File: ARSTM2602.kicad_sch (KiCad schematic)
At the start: 0 parts

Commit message: aaa
gitdesktop test
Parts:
- added U1: STM32H523CCTx, Package_QFP:LQFP-48_7x7mm_P0.5mm, symbol MCU_ST_STM32H5:STM32H523CCTx
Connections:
- new net: U1.23 (VSS), U1.35 (VSS), U1.47 (VSS)
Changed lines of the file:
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@@
 (kicad_sch
-	(version 20250114)
+	(version 20260306)
 	(generator "eeschema")
-	(generator_version "9.0")
+	(generator_version "10.0")
 	(paper "A4")
-	(sheet_instances
-		(path "/"
-			(page "1")
-		)
-	)
-	(embedded_fonts no)
-)

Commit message: 回路図をこぴった
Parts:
- removed U1: STM32H523CCTx, Package_QFP:LQFP-48_7x7mm_P0.5mm, symbol MCU_ST_STM32H5:STM32H523CCTx
- added C1, C17: 22μF, Capacitor_SMD:C_0805_2012Metric_Pad1.18x1.45mm_HandSolder, symbol Device:C
- added C10: 4.7uf, Capacitor_SMD:C_0805_2012Metric_Pad1.18x1.45mm_HandSolder, symbol Device:C
- added C11, C7, C8, C9: 0.1uF, Capacitor_SMD:C_0603_1608Metric_Pad1.08x0.95mm_HandSolder, symbol Device:C
- added C12, C4: 0.1uf, Capacitor_SMD:C_0603_1608Metric_Pad1.08x0.95mm_HandSolder, symbol Device:C
- added C13, C14: 1uf, Capacitor_SMD:C_0603_1608Metric_Pad1.08x0.95mm_HandSolder, symbol Device:C
- added C15, C16, C2, C3: 4.7μF, Capacitor_SMD:C_0805_2012Metric_Pad1.18x1.45mm_HandSolder, symbol Device:C
- added C5, C6: 2.2μF, Capacitor_SMD:C_0603_1608Metric_Pad1.08x0.95mm_HandSolder, symbol Device:C
- added D2, D4: D_Shockley, Diode_SMD:D_SOD-323_HandSoldering, symbol Device:D_Shockley
- added D3: LED_GREEN, Capacitor_SMD:C_0603_1608Metric_Pad1.08x0.95mm_HandSolder, symbol Device:LED
- added J10: USB_C_Receptacle_USB2.0_16P, Connector_USB:USB_C_Receptacle_GCT_USB4105-xx-A_16P_TopMnt_Horizontal, symbol Connector:USB_C_Receptacle_USB2.0_16P
- added J4, J5: Conn_01x02_Socket, Connector_JST:JST_XH_S2B-XH-A-1_1x02_P2.50mm_Horizontal, symbol Connector:Conn_01x02_Socket
- added J9: Conn_ST_STDC14, Connector_PinHeader_1.27mm:PinHeader_2x07_P1.27mm_Vertical, symbol Connector:Conn_ST_STDC14
- added R10, R9: 5.1k, Resistor_SMD:R_0603_1608Metric_Pad0.98x0.95mm_HandSolder, symbol Device:R
- added R4: 120, Resistor_SMD:R_0603_1608Metric_Pad0.98x0.95mm_HandSolder, symbol Device:R
- added R5: 10K, Resistor_SMD:R_0603_1608Metric_Pad0.98x0.95mm_HandSolder, symbol Device:R
- added R7: 1k, Resistor_SMD:R_0603_1608Metric_Pad0.98x0.95mm_HandSolder, symbol Device:R
- added SW1: SW_Wuerth_450301014042, Button_Switch_THT:SW_Slide-03_Wuerth-WS-SLTV_10x2.5x6.4_P2.54mm, symbol Switch:SW_Wuerth_450301014042
- added SW2: SW_SPDT, Button_Switch_THT:SW_Slide-03_Wuerth-WS-SLTV_10x2.5x6.4_P2.54mm, symbol Switch:SW_SPDT
- added SW3: SW_Push, Button_Switch_THT:SW_PUSH_6mm, symbol Switch:SW_Push
- added U1: BD50FC0FP, Package_TO_SOT_SMD:TO-252-2, symbol Regulator_Linear:BD50FC0FP
- added U3: MCP2562-E-P, Package_DIP:DIP-8_W7.62mm, symbol Interface_CAN_LIN:MCP2562-E-P
- added U4: STM32H523CCTx, Package_QFP:LQFP-48_7x7mm_P0.5mm, symbol MCU_ST_STM32H5:STM32H523CCTx
- added U5: BD33FC0FP, Package_TO_SOT_SMD:TO-252-2, symbol Regulator_Linear:BD33FC0FP
- added U6: CH340E, Package_SO:MSOP-10_3x3mm_P0.5mm, symbol Interface_USB:CH340E
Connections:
- new net: D3.1 (K), R7.2
- new net: C6.2, U4.46 (VCAP)
- new net: C5.2, U4.22 (VCAP)
- new net: J10.A5 (CC1), R10.1
- new net: J10.B5 (CC2), R9.1
- new net: D3.2 (A), U4.11 (PA1)
- new net: C14.1, U6.10 (V3)
- new net +24V: C2.1, D2.1 (K), U1.1 (VCC)
- new net +3.3V: C10.1, C11.1, C12.2, C13.2, C16.1, C17.1, C7.1, C8.1, C9.1, D4.2 (A), J9.3 (VCC), U3.5 (Vio), U4.1 (VBAT), U4.24 (VDD), U4.36 (VDD), U4.48 (VDD), U4.9 (VDDA), U5.3 (VO)
- new net +5V: C1.1, C15.1, C3.1, C4.1, D2.2 (A), D4.1 (K), J10.A4 (VBUS), J10.A9 (VBUS), J10.B4 (VBUS), J10.B9 (VBUS), U1.3 (VO), U3.3 (VDD), U5.1 (VCC), U6.7 (VCC)
- new net BOOT0: R5.1, SW2.2 (B), U4.44 (BOOT0)
- new net CAN2rx: U3.4 (RXD), U4.32 (PA11)
- new net CAN2tx: U3.1 (TXD), U4.33 (PA12)
- new net CANR: R4.2, SW1.3 (A)
- new net CAN_H: J4.2 (Pin_2), J5.2 (Pin_2), SW1.1 (B), U3.7 (CANH)
- new net CAN_L: J4.1 (Pin_1), J5.1 (Pin_1), R4.1, U3.6 (CANL)
- new net GND: C1.2, C10.2, C11.2, C12.1, C13.1, C14.2, C15.2, C16.2, C17.2, C2.2, C3.2, C4.2, C5.1, C6.1, C7.2, C8.2, C9.2, J10.A1 (GND), J10.A12 (GND), J10.B1 (GND), J10.B12 (GND), J10.S1 (SHIELD), J9.5 (GND), J9.7 (GND), R10.2, R5.2, R7.1, R9.2, SW2.1 (A), SW3.2, U1.2 (GND), U3.2 (VSS), U3.8 (STBY), U4.23 (VSS), U4.35 (VSS), U4.47 (VSS), U4.8 (VSSA), U5.2 (GND), U6.3 (GND)
- new net d+: J10.A7 (D-), J10.B7 (D-), U6.1 (UD+)
- new net d-: J10.A6 (D+), J10.B6 (D+), U6.2 (UD-)
- new net jtdi: J9.10 (JTDI/NC), U4.38 (PA15(JTDI))
- new net nrst: SW3.1, U4.7 (NRST)
- new net swclk: J9.6 (JCLK/SWCLK), U4.37 (PA14(JTCK)
- new net swdio: J9.4 (JTMS/SWDIO), U4.34 (PA13(JTMS)
- new net swo: J9.8 (JTDO/SWO), U4.39 (PB3(JTDO)
- new net trst: J9.12 (~{RST}), U4.40 (PB4(NJTRST))
- new net uart1-rx: J9.13 (VCP_RX), U4.43 (PB7), U6.9 (RXD)
- new net uart1-tx: J9.14 (VCP_TX), U4.42 (PB6), U6.8 (TXD)
- no-connect marks 0 -> 9
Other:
- note added: "CANトランシーバー"
- note added: "STlink,電源供給usbC"
- note added: "リセット用スイッチ"
- note added: "終端抵抗オンオフ"

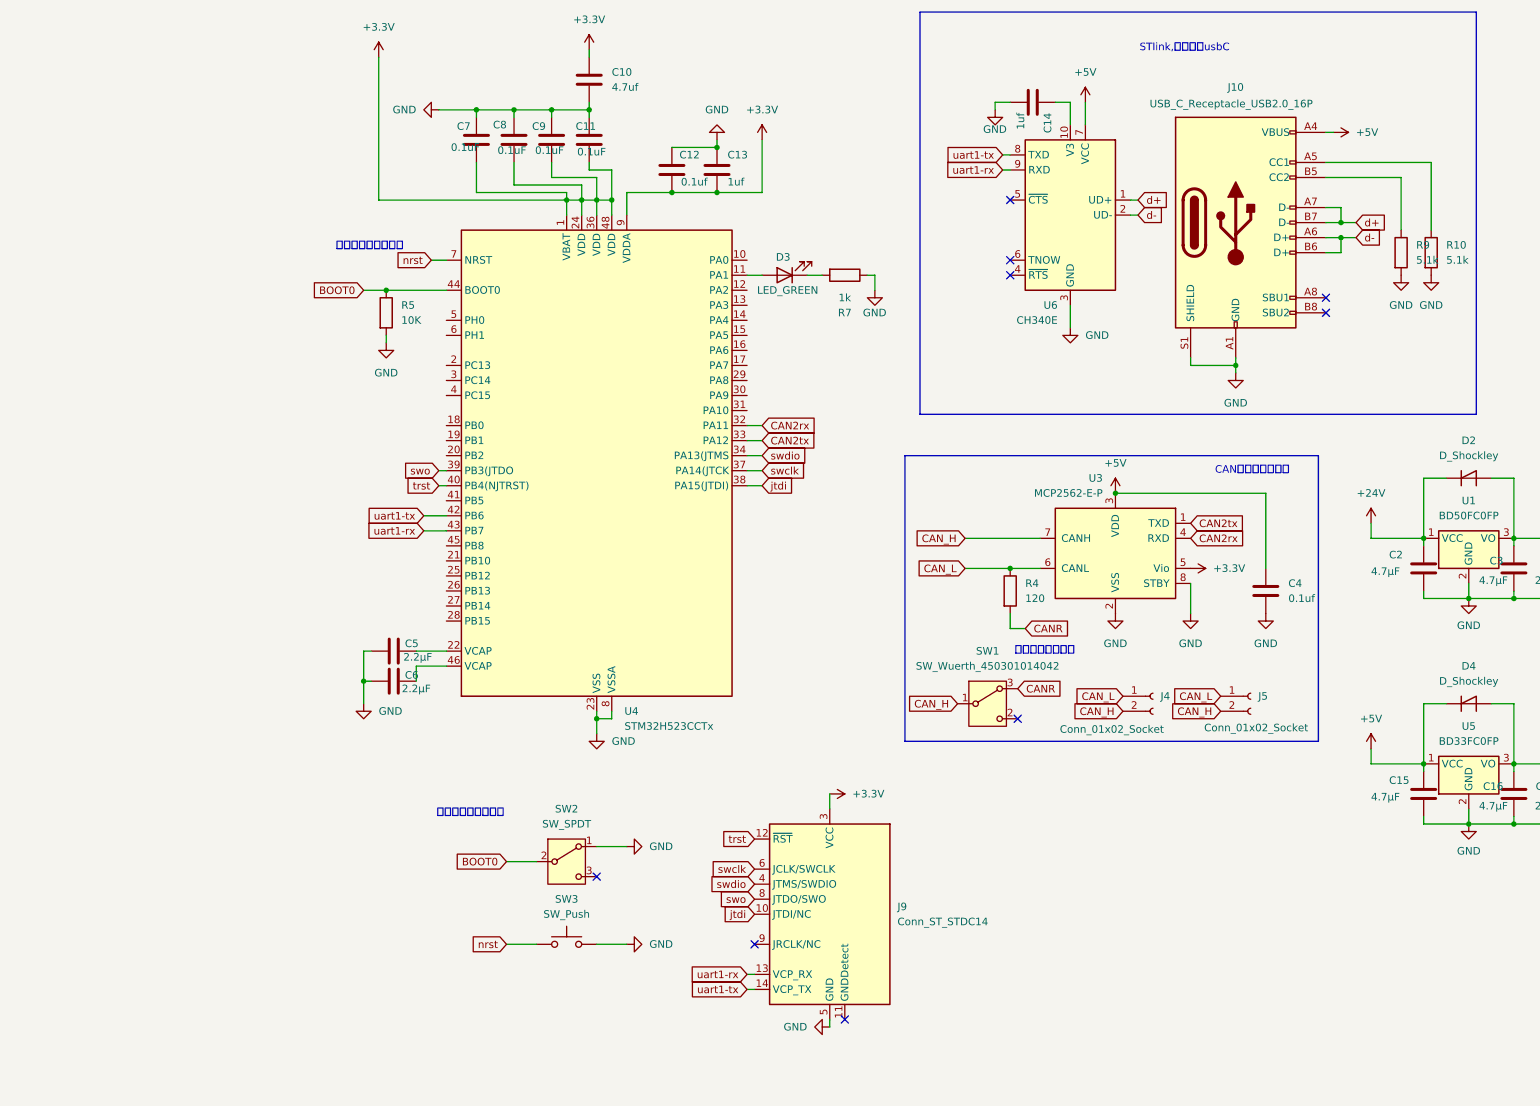
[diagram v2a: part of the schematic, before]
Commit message: canモジュールを増やした
電源供給方法をいろいろ考えついたから頑張る()
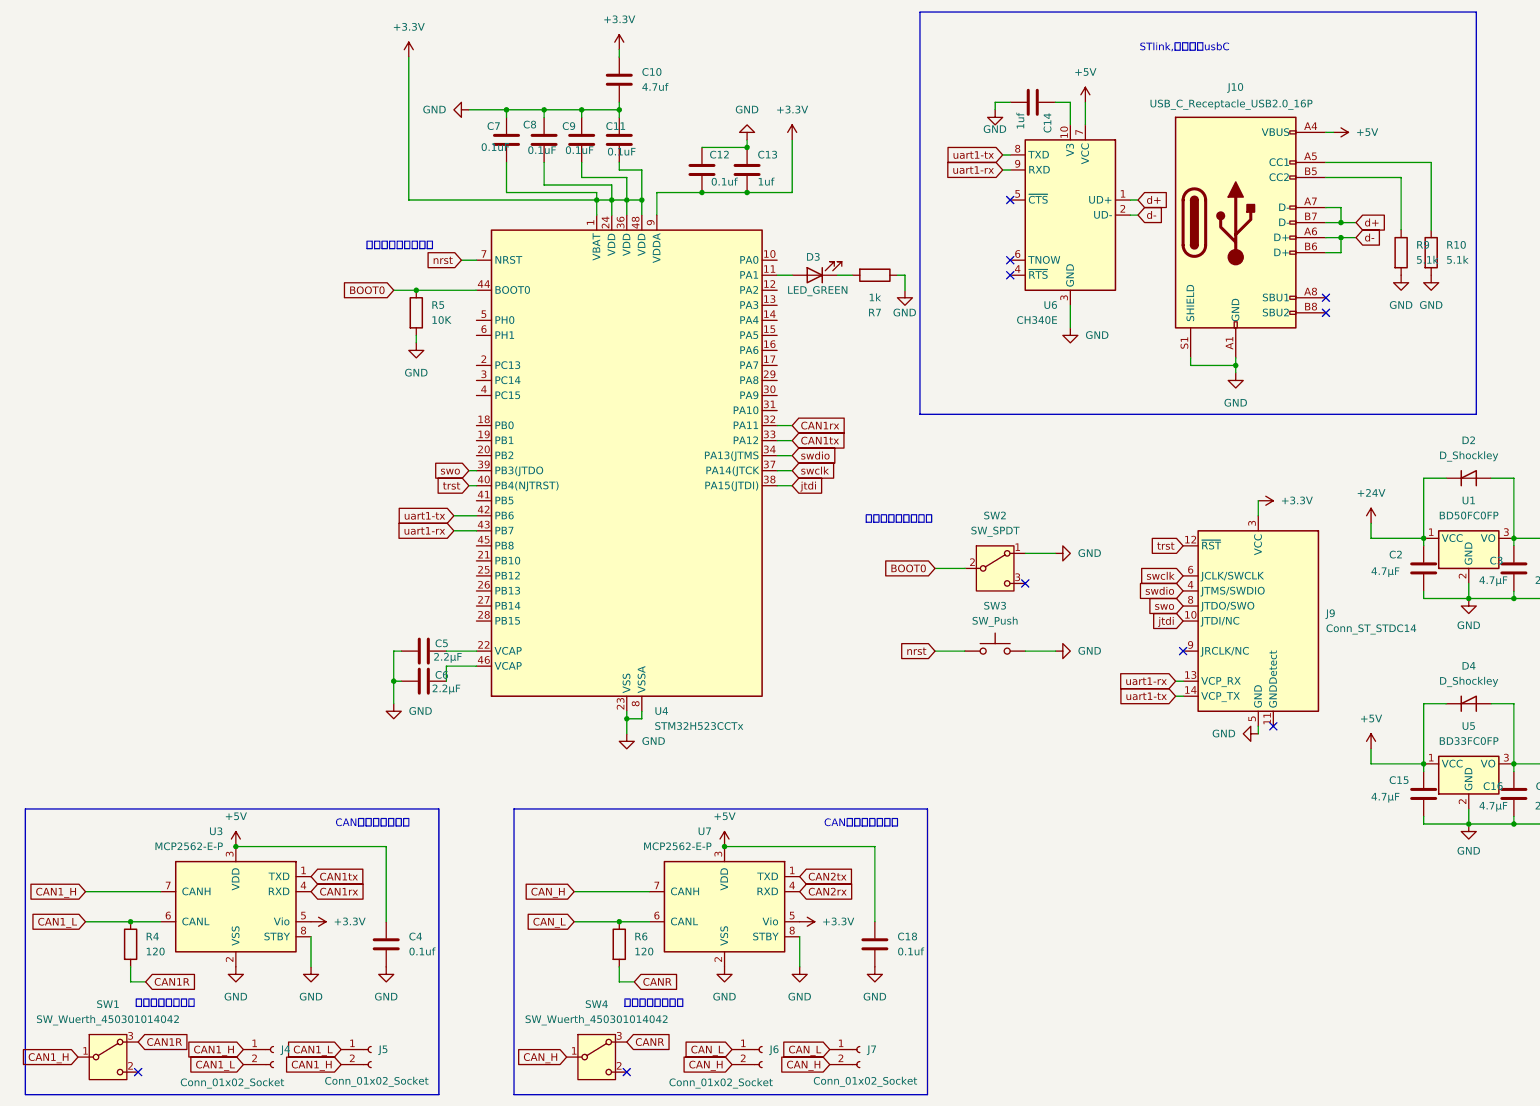
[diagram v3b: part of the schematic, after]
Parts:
- added C18: 0.1uf, Capacitor_SMD:C_0603_1608Metric_Pad1.08x0.95mm_HandSolder, symbol Device:C
- added J6, J7: Conn_01x02_Socket, Connector_JST:JST_XH_S2B-XH-A-1_1x02_P2.50mm_Horizontal, symbol Connector:Conn_01x02_Socket
- added R6: 120, Resistor_SMD:R_0603_1608Metric_Pad0.98x0.95mm_HandSolder, symbol Device:R
- added SW4: SW_Wuerth_450301014042, Button_Switch_THT:SW_Slide-03_Wuerth-WS-SLTV_10x2.5x6.4_P2.54mm, symbol Switch:SW_Wuerth_450301014042
- added U7: MCP2562-E-P, Package_DIP:DIP-8_W7.62mm, symbol Interface_CAN_LIN:MCP2562-E-P
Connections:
- net +3.3V: now also U7.5 (Vio)
- net +5V: now also C18.1, U7.3 (VDD)
- net CAN2rx: now also U7.4 (RXD); no longer U3.4 (RXD), U4.32 (PA11)
- net CAN2tx: now also U7.1 (TXD); no longer U3.1 (TXD), U4.33 (PA12)
- net CANR: now also R6.2, SW4.3 (A); no longer R4.2, SW1.3 (A)
- net CAN_H: now also J6.2 (Pin_2), J7.2 (Pin_2), SW4.1 (B), U7.7 (CANH); no longer J4.2 (Pin_2), J5.2 (Pin_2), SW1.1 (B), U3.7 (CANH)
- net CAN_L: now also J6.1 (Pin_1), J7.1 (Pin_1), R6.1, U7.6 (CANL); no longer J4.1 (Pin_1), J5.1 (Pin_1), R4.1, U3.6 (CANL)
- net GND: now also C18.2, U7.2 (VSS), U7.8 (STBY)
- new net CAN1R: R4.2, SW1.3 (A)
- new net CAN1_H: J4.1 (Pin_1), J5.2 (Pin_2), SW1.1 (B), U3.7 (CANH)
- new net CAN1_L: J4.2 (Pin_2), J5.1 (Pin_1), R4.1, U3.6 (CANL)
- new net CAN1rx: U3.4 (RXD), U4.32 (PA11)
- new net CAN1tx: U3.1 (TXD), U4.33 (PA12)
- no-connect marks 9 -> 10
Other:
- moved on the sheet: C10, C11, C12, C13, C4, C5, C6, C7, C8, C9, D3, J4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

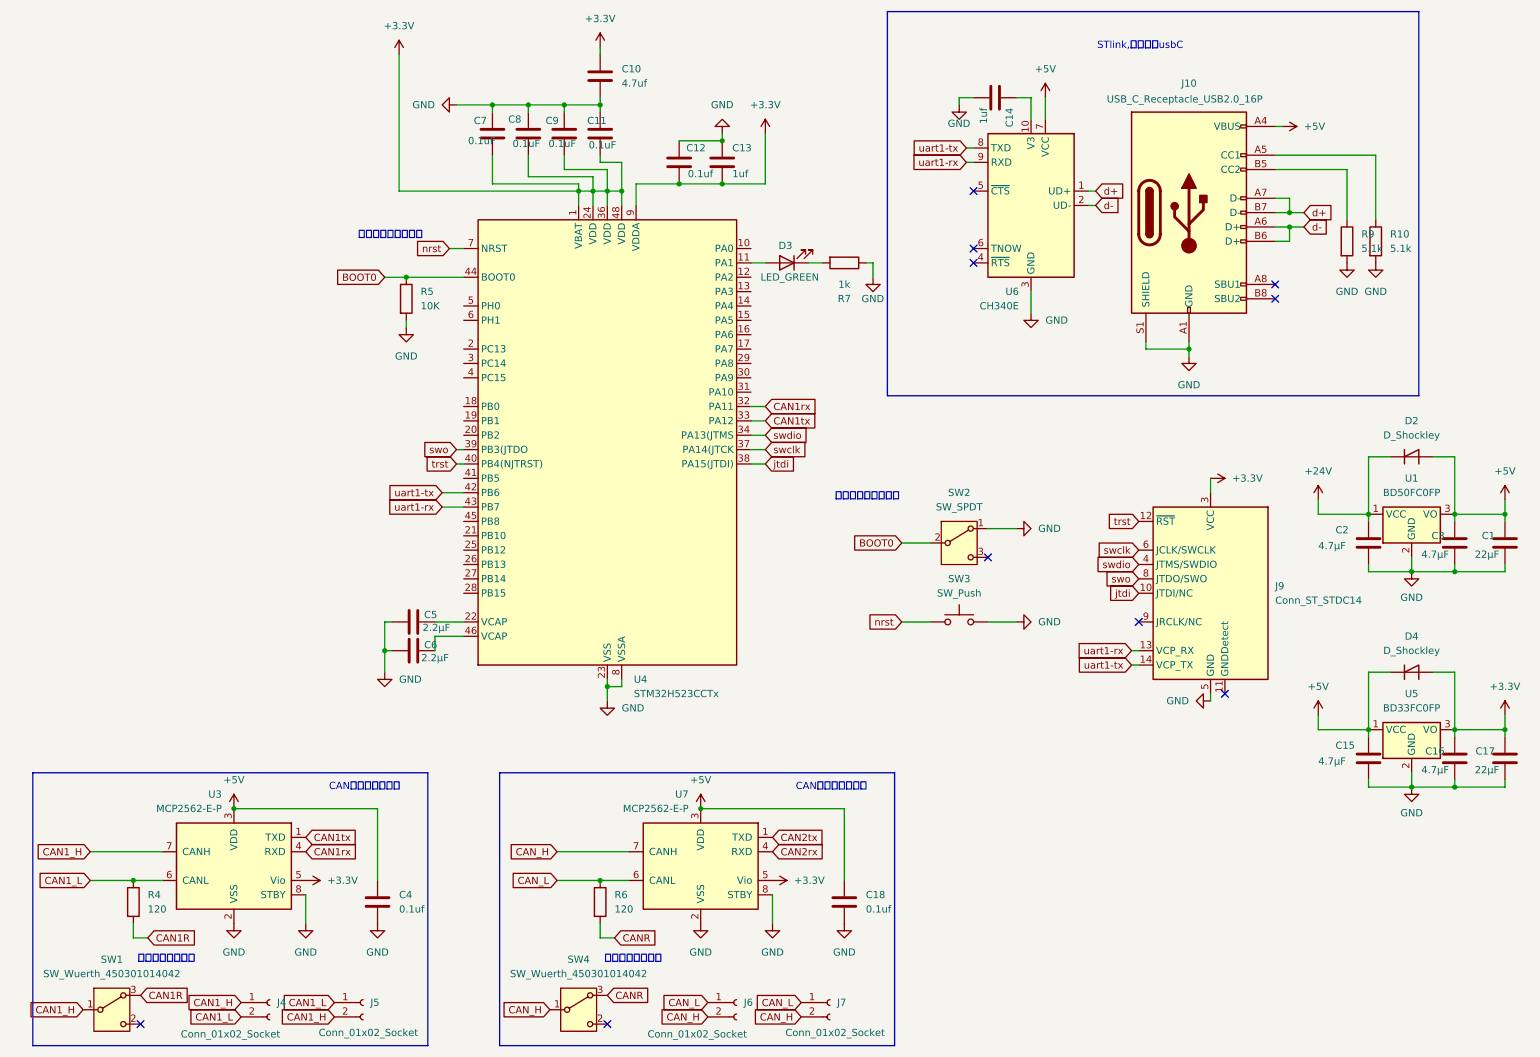
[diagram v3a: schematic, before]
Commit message: canモジュールの置き換え
tcan3414に置き換えた
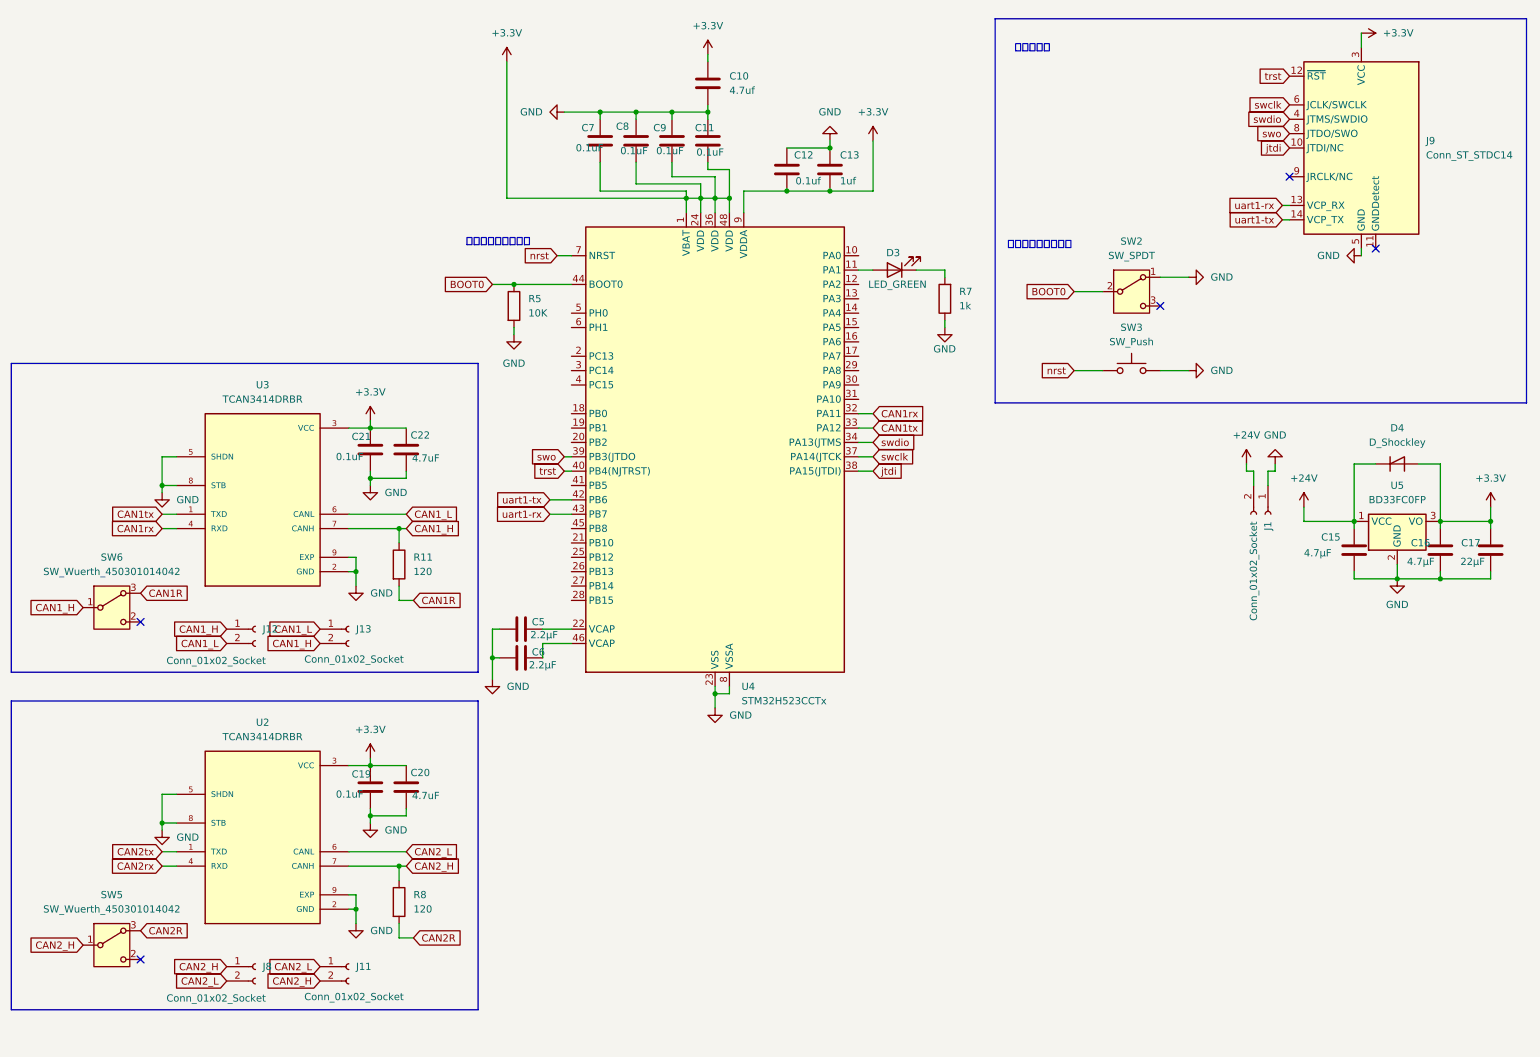
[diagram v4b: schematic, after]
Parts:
- removed C1: 22μF, Capacitor_SMD:C_0805_2012Metric_Pad1.18x1.45mm_HandSolder, symbol Device:C
- removed C14: 1uf, Capacitor_SMD:C_0603_1608Metric_Pad1.08x0.95mm_HandSolder, symbol Device:C
- removed C18, C4: 0.1uf, Capacitor_SMD:C_0603_1608Metric_Pad1.08x0.95mm_HandSolder, symbol Device:C
- removed C2, C3: 4.7μF, Capacitor_SMD:C_0805_2012Metric_Pad1.18x1.45mm_HandSolder, symbol Device:C
- removed D2: D_Shockley, Diode_SMD:D_SOD-323_HandSoldering, symbol Device:D_Shockley
- removed J10: USB_C_Receptacle_USB2.0_16P, Connector_USB:USB_C_Receptacle_GCT_USB4105-xx-A_16P_TopMnt_Horizontal, symbol Connector:USB_C_Receptacle_USB2.0_16P
- removed J4, J5, J6, J7: Conn_01x02_Socket, Connector_JST:JST_XH_S2B-XH-A-1_1x02_P2.50mm_Horizontal, symbol Connector:Conn_01x02_Socket
- removed R10, R9: 5.1k, Resistor_SMD:R_0603_1608Metric_Pad0.98x0.95mm_HandSolder, symbol Device:R
- removed R4, R6: 120, Resistor_SMD:R_0603_1608Metric_Pad0.98x0.95mm_HandSolder, symbol Device:R
- removed SW1, SW4: SW_Wuerth_450301014042, Button_Switch_THT:SW_Slide-03_Wuerth-WS-SLTV_10x2.5x6.4_P2.54mm, symbol Switch:SW_Wuerth_450301014042
- removed U1: BD50FC0FP, Package_TO_SOT_SMD:TO-252-2, symbol Regulator_Linear:BD50FC0FP
- removed U3, U7: MCP2562-E-P, Package_DIP:DIP-8_W7.62mm, symbol Interface_CAN_LIN:MCP2562-E-P
- removed U6: CH340E, Package_SO:MSOP-10_3x3mm_P0.5mm, symbol Interface_USB:CH340E
- added C19, C21: 0.1uF, Capacitor_SMD:C_0603_1608Metric_Pad1.08x0.95mm_HandSolder, symbol Device:C
- added C20, C22: 4.7uF, Capacitor_SMD:C_0603_1608Metric_Pad1.08x0.95mm_HandSolder, symbol Device:C
- added J1: Conn_01x02_Socket, Connector_AMASS:AMASS_XT30PW-M_1x02_P2.50mm_Horizontal, symbol Connector:Conn_01x02_Socket
- added J11, J12, J13, J8: Conn_01x02_Socket, Connector_JST:JST_XH_S2B-XH-A-1_1x02_P2.50mm_Horizontal, symbol Connector:Conn_01x02_Socket
- added R11, R8: 120, Resistor_SMD:R_0603_1608Metric_Pad0.98x0.95mm_HandSolder, symbol Device:R
- added SW5, SW6: SW_Wuerth_450301014042, Button_Switch_THT:SW_Slide-03_Wuerth-WS-SLTV_10x2.5x6.4_P2.54mm, symbol Switch:SW_Wuerth_450301014042
- added U2, U3: TCAN3414DRBR, TCAN3414DRBR:XCVR_TCAN3414DRBR, symbol TCAN3414DRBR:TCAN3414DRBR
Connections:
- net +5V is gone; now on net +24V: C15.1, D4.1 (K), U5.1 (VCC)
- net +24V: now also J1.2 (Pin_2)
- net +3.3V: now also C19.2, C20.2, C21.2, C22.2, U2.3 (VCC), U3.3 (VCC)
- net CAN1R: now also R11.2, SW6.3 (A)
- net CAN1_H: now also J12.1 (Pin_1), J13.2 (Pin_2), R11.1, SW6.1 (B), U3.7 (CANH)
- net CAN1_L: now also J12.2 (Pin_2), J13.1 (Pin_1), U3.6 (CANL)
- net CAN1rx: now also U3.4 (RXD)
- net CAN1tx: now also U3.1 (TXD)
- net CAN2rx: now also U2.4 (RXD)
- net CAN2tx: now also U2.1 (TXD)
- net GND: now also C19.1, C20.1, C21.1, C22.1, J1.1 (Pin_1), U2.2 (GND), U2.5 (SHDN), U2.8 (STB), U2.9 (EXP), U3.2 (GND), U3.5 (SHDN), U3.8 (STB), U3.9 (EXP)
- new net CAN2R: R8.2, SW5.3 (A)
- new net CAN2_H: J11.2 (Pin_2), J8.1 (Pin_1), R8.1, SW5.1 (B), U2.7 (CANH)
- new net CAN2_L: J11.1 (Pin_1), J8.2 (Pin_2), U2.6 (CANL)
- no-connect marks 10 -> 5
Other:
- note added: "デバッグ系"
- note removed: "CANトランシーバー"
- note removed: "STlink,電源供給usbC"
- note removed: "終端抵抗オンオフ"
- moved on the sheet: C10, C11, C12, C13, C15, C16, C17, C5, C6, C7, C8, C9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
